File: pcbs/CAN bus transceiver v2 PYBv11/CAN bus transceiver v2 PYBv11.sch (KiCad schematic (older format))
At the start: 20 parts, among them P1 CONN_01X06, P2 CONN_01X02, P3 CONN_01X06, P4 CONN_01X02, Q1 Q_PMOS_SGD, U1 TCAN337GDR, U2 TCAN337GDR, U3 LM3489

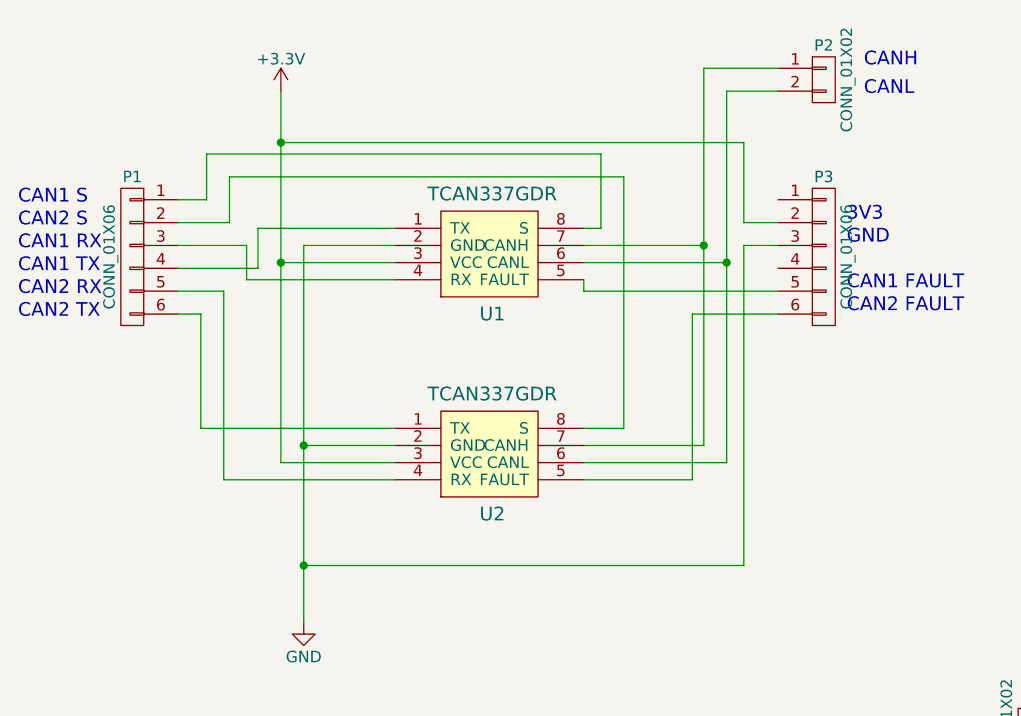
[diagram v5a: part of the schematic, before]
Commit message: can: placing LM3489 components on board
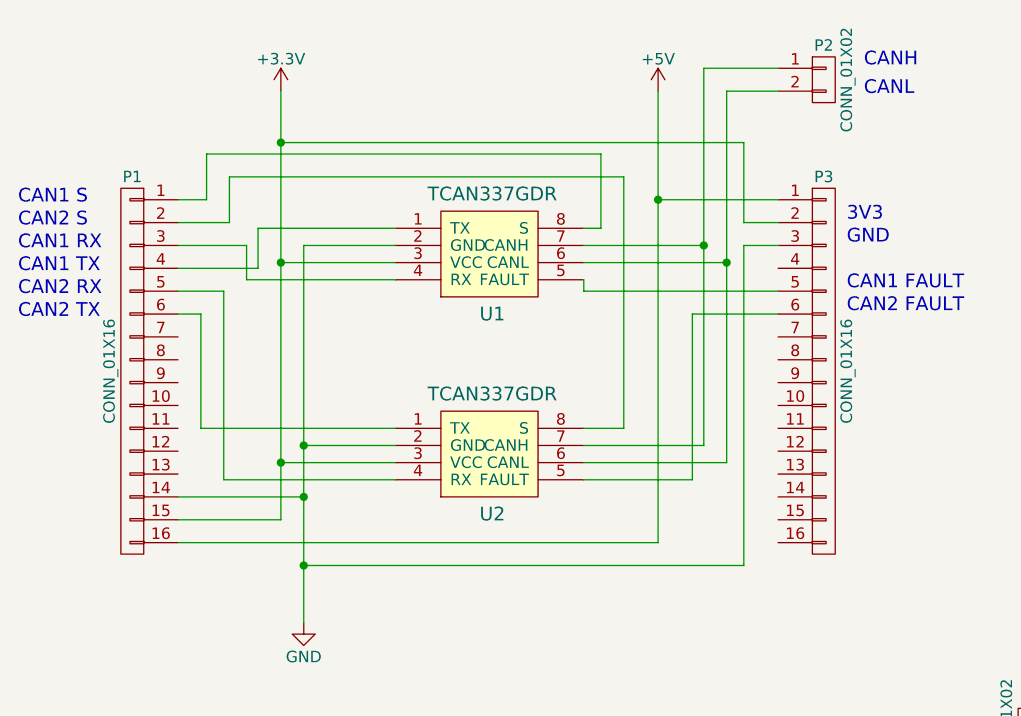
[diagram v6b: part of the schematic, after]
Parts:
- removed P1, P3: CONN_01X06, Pin_Headers:Pin_Header_Straight_1x06, symbol CONN_01X06
- added P1, P3: CONN_01X16, Pin_Headers:Pin_Header_Straight_1x16, symbol CONN_01X16
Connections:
- net +3V3: now also P1.15 (P15), P3.2 (P2)
- net +5V: now also P1.16 (P16), P3.1 (P1)
- net GND: now also P1.14 (P14), P3.3 (P3)
- net at U1.1 (TX): now also P1.4 (P4)
- net at U1.4 (RX): now also P1.3 (P3)
- net at U1.5 (FAULT): now also P3.5 (P5)
- net at U1.8 (S): now also P1.1 (P1)
- net at U2.1 (TX): now also P1.6 (P6)
- net at U2.4 (RX): now also P1.5 (P5)
- net at U2.5 (FAULT): now also P3.6 (P6)
- net at U2.8 (S): now also P1.2 (P2)
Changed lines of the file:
@@
 CAN2 TX
 $Comp
-L GND #PWR2
+L GND #PWR01
 U 1 1 58129EE2
 P 1775 3125
-F 0 "#PWR2" H 1775 2875 50  0001 C CNN
+F 0 "#PWR01" H 1775 2875 50  0001 C CNN
 F 1 "GND" H 1775 2975 50  0000 C CNN
 F 2 "" H 1775 3125 50  0000 C CNN
@@
 $EndComp
 $Comp
-L +3.3V #PWR1
+L +3.3V #PWR02
 U 1 1 58129EFE
 P 1675 800
-F 0 "#PWR1" H 1675 650 50  0001 C CNN
+F 0 "#PWR02" H 1675 650 50  0001 C CNN
 F 1 "+3.3V" H 1675 940 50  0000 C CNN
 F 2 "" H 1675 800 50  0000 C CNN
@@
 Text Notes 4225 825  0    60   ~ 0
 CANL
-$Comp
-L CONN_01X06 P1
-U 1 1 58144AB1
-P 1025 1525
-F 0 "P1" H 1025 1875 50  0000 C CNN
-F 1 "CONN_01X06" V 1125 1525 50  0000 C CNN
-F 2 "Pin_Headers:Pin_Header_Straight_1x06" H 1025 1525 50  0001 C CNN
-F 3 "" H 1025 1525 50  0000 C CNN
-	1    1025 1525
-	-1   0    0    -1
-$EndComp
-$Comp
-L CONN_01X06 P3
-U 1 1 58144C08
-P 4050 1525
-F 0 "P3" H 4050 1875 50  0000 C CNN
-F 1 "CONN_01X06" V 4150 1525 50  0000 C CNN
-F 2 "Pin_Headers:Pin_Header_Straight_1x06" H 4050 1525 50  0001 C CNN
-F 3 "" H 4050 1525 50  0000 C CNN
-	1    4050 1525
-	1    0    0    -1
-$EndComp
 Text Notes 4150 1675 0    60   ~ 0
 CAN1 FAULT
@@
 $EndComp
 $Comp
-L +12V #PWR3
+L +12V #PWR03
 U 1 1 582E542A
 P 5200 3175
-F 0 "#PWR3" H 5200 3025 50  0001 C CNN
+F 0 "#PWR03" H 5200 3025 50  0001 C CNN
 F 1 "+12V" H 5200 3315 50  0000 C CNN
 F 2 "" H 5200 3175 50  0000 C CNN
@@
 $EndComp
 $Comp
-L GND #PWR4
+L GND #PWR04
 U 1 1 582E5458
 P 5200 4075
-F 0 "#PWR4" H 5200 3825 50  0001 C CNN
+F 0 "#PWR04" H 5200 3825 50  0001 C CNN
 F 1 "GND" H 5200 3925 50  0000 C CNN
 F 2 "" H 5200 4075 50  0000 C CNN
@@
 	1775 1475 1775 3125
 Wire Wire Line
-	1675 2425 1675 800
+	1675 800  1675 2675
 Wire Wire Line
 	5150 3550 5200 3550
@@
 Connection ~ 7700 3425
 $Comp
-L +5V #PWR5
+L +5V #PWR05
 U 1 1 582E8FD4
 P 10575 3075
-F 0 "#PWR5" H 10575 2925 50  0001 C CNN
+F 0 "#PWR05" H 10575 2925 50  0001 C CNN
 F 1 "+5V" H 10575 3215 50  0000 C CNN
 F 2 "" H 10575 3075 50  0000 C CNN
@@
 	5500 3800 5500 4050
 Connection ~ 5500 4050
+$Comp
+L CONN_01X16 P3
+U 1 1 58324F2F
+P 4050 2025
+F 0 "P3" H 4050 2875 50  0000 C CNN
+F 1 "CONN_01X16" V 4150 2025 50  0000 C CNN
+F 2 "Pin_Headers:Pin_Header_Straight_1x16" H 4050 2025 50  0001 C CNN
+F 3 "" H 4050 2025 50  0000 C CNN
+	1    4050 2025
+	1    0    0    -1
+$EndComp
+$Comp
+L CONN_01X16 P1
+U 1 1 58325137
+P 1025 2025
+F 0 "P1" H 1025 2875 50  0000 C CNN
+F 1 "CONN_01X16" V 1125 2025 50  0000 C CNN
+F 2 "Pin_Headers:Pin_Header_Straight_1x16" H 1025 2025 50  0001 C CNN
+F 3 "" H 1025 2025 50  0000 C CNN
+	1    1025 2025
+	-1   0    0    -1
+$EndComp
+$Comp
+L +5V #PWR06
+U 1 1 583255A6
+P 3325 800
+F 0 "#PWR06" H 3325 650 50  0001 C CNN
+F 1 "+5V" H 3325 940 50  0000 C CNN
+F 2 "" H 3325 800 50  0000 C CNN
+F 3 "" H 3325 800 50  0000 C CNN
+	1    3325 800
+	1    0    0    -1
+$EndComp
+Wire Wire Line
+	3850 1275 3325 1275
+Wire Wire Line
+	3325 800  3325 2775
+Wire Wire Line
+	3325 2775 1225 2775
+Connection ~ 3325 1275
+Wire Wire Line
+	1675 2675 1225 2675
+Connection ~ 1675 2425
+Wire Wire Line
+	1225 2575 1775 2575
+Connection ~ 1775 2575
 $EndSCHEMATC

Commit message: can: changed Zenner diode footprint
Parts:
- D1: footprint Diodes_SMD:SMB_Handsoldering -> Diodes_SMD:SOD-523
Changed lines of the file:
@@
 F 0 "D1" H 5500 3700 50  0000 C CNN
 F 1 "ZENER" H 5500 3500 50  0000 C CNN
-F 2 "Diodes_SMD:SMB_Handsoldering" H 5500 3600 50  0001 C CNN
+F 2 "Diodes_SMD:SOD-523" H 5500 3600 50  0001 C CNN
 F 3 "" H 5500 3600 50  0000 C CNN
 	1    5500 3600
